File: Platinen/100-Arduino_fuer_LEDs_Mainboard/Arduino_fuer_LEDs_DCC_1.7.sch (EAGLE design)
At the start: 115 parts, among them IC1 7805, IC2 LM393N, J1 Tag/Nacht, U1 WS2812_MODUL, U2 LED NANO, U3 DCC NANO, U4 WS2812_MODUL, X1 RJ10, X2 AK500/2+M, X3 MAB 5SH Conrad: 738247 - VQ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

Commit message: New Mainboard V.:1.7
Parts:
- added IC3: 74LVC1G125DBV, 74xx-little-de:74LVC1G125DBV
- added R2: 47, rcl:R-EU_0204/7
- added R9: 10K, rcl:R-EU_0204/5
- added SJ2: SOLDERJUMPERNO, SparkFun-Retired:SOLDERJUMPERNO
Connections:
- removed net N$53: O4.4
- new net N$22: O3.4, O4.2
- new net N$31: IC3A.I, R26.2, SJ2.1, U3.TX0
- new net N$33: IC3A.O, R2.1
- new net N$34: R2.2, SJ2.2, U2.RX1
- net +5V: now also R9.2
- net N$3: now also IC3A.OE, R9.1, U3.A5; no longer R26.2, U2.RX1, U3.TX0
- net N$52: now also O4.4; no longer O3.4, O4.2
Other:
- note added: "Revision History: 31.08.20: - Corrected the LED PCBs (Ver. 1.5 was totaly wrong) - swaped the Input/Output pins (3-Pin header = Input) - corrected the pin assignement of the 3535 WS2812 18.10.20: - Corrected the output of the last connector"
- note added: "SJ2 ist normalerweise verbunden. IC3, R2 und R9 können anstelle von R26 bestückt werden. Dann bleibt SJ2 offen. (Noch nicht getestet)"
- note added: "Ver.: 1.7"
- note removed: "Revision History: 31.08.20: - Corrected the LED PCBs (Ver. 1.5 was totaly wrong) - swaped the Input/Output pins (3-Pin header = Input) - corrected the pin assignement of the 3535 WS2812"
- note removed: "Ver.: 1.6"
- moved on the sheet: IC2A, IC2B, R21, R22, R23, R24, R25, R26, R28, SJ_SX1, SJ_SX2, SJ_SX3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

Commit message: Moved IC3
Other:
- note added: "Achtung: Selectrix Empfang funktioniert NICHT wenn der DCC Optokoppler OK1 eingesteckt ist!"
- note added: "Ver.: 1.7.1"
- note added: "Wenn die Platine aus dem DCC Signal versorgt wird (IC1... bestückt), dann kann OK1 entfallen. Stattdessen wird eine Diode Pin3 nach Pin2 verwendet und NO_OPTO verbunden. R8 muss dann mit 33K bestückt werden. (Noch nicht getestet)"
- note removed: "Ver.: 1.7"
- note removed: "Wenn die Platine aus dem DCC Signal versorgt wird (IC1... bestückt), dann kann OK1 entfallen. Stattdessen wird eine Diode Pin3 nach Pin2 verwendet und NO_OPTO verbunden."
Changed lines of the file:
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@@
 <grid distance="0.1" unitdist="inch" unit="inch" style="lines" multiple="1" display="no" altdistance="0.05" altunitdist="inch" altunit="inch"/>
 <layers>
-<layer number="1" name="Top" color="4" fill="1" visible="yes" active="no"/>
-<layer number="16" name="Bottom" color="1" fill="1" visible="yes" active="no"/>
-<layer number="17" name="Pads" color="2" fill="1" visible="yes" active="no"/>
-<layer number="18" name="Vias" color="2" fill="1" visible="yes" active="no"/>
-<layer number="19" name="Unrouted" color="6" fill="1" visible="yes" active="no"/>
-<layer number="20" name="Dimension" color="24" fill="1" visible="yes" active="no"/>
-<layer number="21" name="tPlace" color="7" fill="1" visible="yes" active="no"/>
-<layer number="22" name="bPlace" color="7" fill="1" visible="yes" active="no"/>
-<layer number="23" name="tOrigins" color="15" fill="1" visible="yes" active="no"/>
-<layer number="24" name="bOrigins" color="15" fill="1" visible="yes" active="no"/>
-<layer number="25" name="tNames" color="7" fill="1" visible="yes" active="no"/>
-<layer number="26" name="bNames" color="7" fill="1" visible="yes" active="no"/>
-<layer number="27" name="tValues" color="7" fill="1" visible="yes" active="no"/>
-<layer number="28" name="bValues" color="7" fill="1" visible="yes" active="no"/>
+<layer number="1" name="Top" color="4" fill="1" visible="no" active="no"/>
+<layer number="16" name="Bottom" color="1" fill="1" visible="no" active="no"/>
+<layer number="17" name="Pads" color="2" fill="1" visible="no" active="no"/>
+<layer number="18" name="Vias" color="2" fill="1" visible="no" active="no"/>
+<layer number="19" name="Unrouted" color="6" fill="1" visible="no" active="no"/>
+<layer number="20" name="Dimension" color="24" fill="1" visible="no" active="no"/>
+<layer number="21" name="tPlace" color="7" fill="1" visible="no" active="no"/>
+<layer number="22" name="bPlace" color="7" fill="1" visible="no" active="no"/>
+<layer number="23" name="tOrigins" color="15" fill="1" visible="no" active="no"/>
+<layer number="24" name="bOrigins" color="15" fill="1" visible="no" active="no"/>
+<layer number="25" name="tNames" color="7" fill="1" visible="no" active="no"/>
+<layer number="26" name="bNames" color="7" fill="1" visible="no" active="no"/>
+<layer number="27" name="tValues" color="7" fill="1" visible="no" active="no"/>
+<layer number="28" name="bValues" color="7" fill="1" visible="no" active="no"/>
 <layer number="29" name="tStop" color="7" fill="3" visible="no" active="no"/>
 <layer number="30" name="bStop" color="7" fill="6" visible="no" active="no"/>
@@
 <layer number="35" name="tGlue" color="7" fill="4" visible="no" active="no"/>
 <layer number="36" name="bGlue" color="7" fill="5" visible="no" active="no"/>
-<layer number="37" name="tTest" color="7" fill="1" visible="yes" active="no"/>
-<layer number="38" name="bTest" color="7" fill="1" visible="yes" active="no"/>
+<layer number="37" name="tTest" color="7" fill="1" visible="no" active="no"/>
+<layer number="38" name="bTest" color="7" fill="1" visible="no" active="no"/>
 <layer number="39" name="tKeepout" color="4" fill="11" visible="no" active="no"/>
 <layer number="40" name="bKeepout" color="1" fill="11" visible="no" active="no"/>
@@
 <layer number="44" name="Drills" color="7" fill="1" visible="no" active="no"/>
 <layer number="45" name="Holes" color="7" fill="1" visible="no" active="no"/>
-<layer number="46" name="Milling" color="3" fill="1" visible="yes" active="no"/>
-<layer number="47" name="Measures" color="7" fill="1" visible="yes" active="no"/>
-<layer number="48" name="Document" color="7" fill="1" visible="yes" active="no"/>
-<layer number="49" name="Reference" color="7" fill="1" visible="yes" active="no"/>
-<layer number="50" name="dxf" color="7" fill="1" visible="yes" active="no"/>
-<layer number="51" name="tDocu" color="7" fill="1" visible="yes" active="no"/>
-<layer number="52" name="bDocu" color="7" fill="1" visible="yes" active="no"/>
-<layer number="53" name="tGND_GNDA" color="7" fill="9" visible="yes" active="no"/>
-<layer number="54" name="bGND_GNDA" color="1" fill="9" visible="yes" active="no"/>
-<layer number="56" name="wert" color="7" fill="1" visible="yes" active="no"/>
-<layer number="57" name="tCAD" color="7" fill="1" visible="yes" active="no"/>
-<layer number="59" name="tCarbon" color="7" fill="1" visible="yes" active="no"/>
-<layer number="60" name="bCarbon" color="7" fill="1" visible="yes" active="no"/>
+<layer number="46" name="Milling" color="3" fill="1" visible="no" active="no"/>
+<layer number="47" name="Measures" color="7" fill="1" visible="no" active="no"/>
+<layer number="48" name="Document" color="7" fill="1" visible="no" active="no"/>
+<layer number="49" name="Reference" color="7" fill="1" visible="no" active="no"/>
+<layer number="50" name="dxf" color="7" fill="1" visible="no" active="no"/>
+<layer number="51" name="tDocu" color="7" fill="1" visible="no" active="no"/>
+<layer number="52" name="bDocu" color="7" fill="1" visible="no" active="no"/>
+<layer number="53" name="tGND_GNDA" color="7" fill="9" visible="no" active="no"/>
+<layer number="54" name="bGND_GNDA" color="1" fill="9" visible="no" active="no"/>
+<layer number="56" name="wert" color="7" fill="1" visible="no" active="no"/>
+<layer number="57" name="tCAD" color="7" fill="1" visible="no" active="no"/>
+<layer number="59" name="tCarbon" color="7" fill="1" visible="no" active="no"/>
+<layer number="60" name="bCarbon" color="7" fill="1" visible="no" active="no"/>
 <layer number="88" name="SimResults" color="9" fill="1" visible="yes" active="yes"/>
 <layer number="89" name="SimProbes" color="9" fill="1" visible="yes" active="yes"/>
@@
 <text x="48.26" y="121.92" size="1.778" layer="97" rot="R90">A6, A7: No Din/Dout
             No Pullup</text>
-<text x="238.76" y="-15.24" size="3.81" layer="97">Ver.: 1.7</text>
+<text x="238.76" y="-15.24" size="3.81" layer="97">Ver.: 1.7.1</text>
 <wire x1="-81.28" y1="198.12" x2="-81.28" y2="200.66" width="0.1524" layer="97"/>
 <wire x1="-81.28" y1="200.66" x2="-82.042" y2="201.422" width="0.1524" layer="97"/>
@@
                =&gt; Ver. 1.6
 10.09.20: - Changed LM293 comment
-18.10.20: - Added optional buffer IC3</text>
+18.10.20: - Added optional buffer IC3
+29.01.21: =&gt; Vwr.: 1.7.1
+                - moved IC3 (problem with narrow pads)</text>
 <text x="-91.44" y="31.75" size="1.778" layer="91">O2</text>
 <text x="-91.44" y="16.51" size="1.778" layer="91">O1</text>
@@
 SJ_SX3 verbinden wenn die Platine aus dem SX Bus versorgt werden soll.
 Das geht aber nur bei wenigen LEDs.</text>
-<text x="-68.58" y="83.82" size="1.524" layer="97" align="top-left">Wenn die Platine aus dem DCC Signal versorgt wird (IC1... bestückt),
+<text x="-68.58" y="86.36" size="1.524" layer="97" align="top-left">Wenn die Platine aus dem DCC Signal versorgt wird (IC1... bestückt),
 dann kann OK1 entfallen. Stattdessen wird eine Diode Pin3 nach Pin2
-verwendet und NO_OPTO verbunden.</text>
+verwendet und NO_OPTO verbunden.
+R8 muss dann mit 33K bestückt werden. (Noch nicht getestet)</text>
 <text x="113.03" y="36.83" size="1.778" layer="97">Achtung: der LM293N
 kann NICHT benutzt
@@
 (Noch nicht getestet)
 </text>
+<text x="33.02" y="-12.7" size="1.524" layer="97" align="top-left">Achtung: Selectrix Empfang funktioniert
+NICHT wenn der DCC Optokoppler OK1
+eingesteckt ist!
+</text>
 </plain>

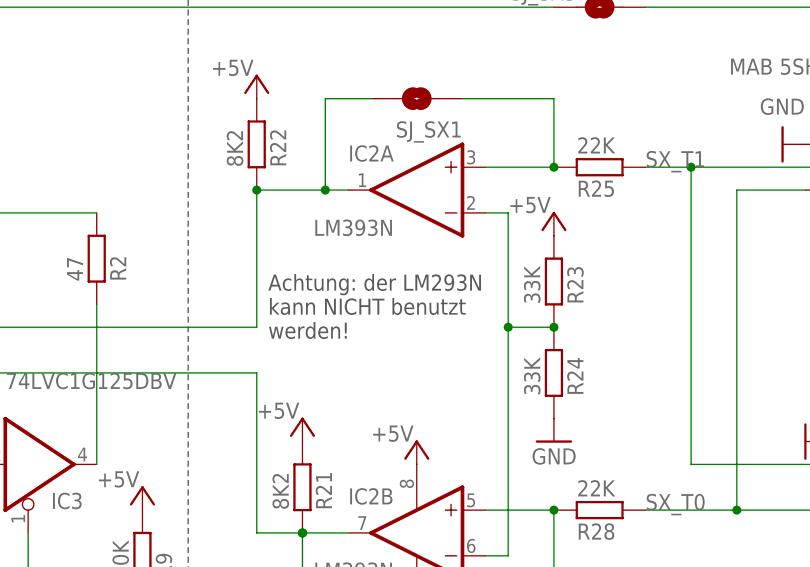
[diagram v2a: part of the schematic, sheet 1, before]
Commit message: Korrigiert: LM292 kann nicht verwendet werden
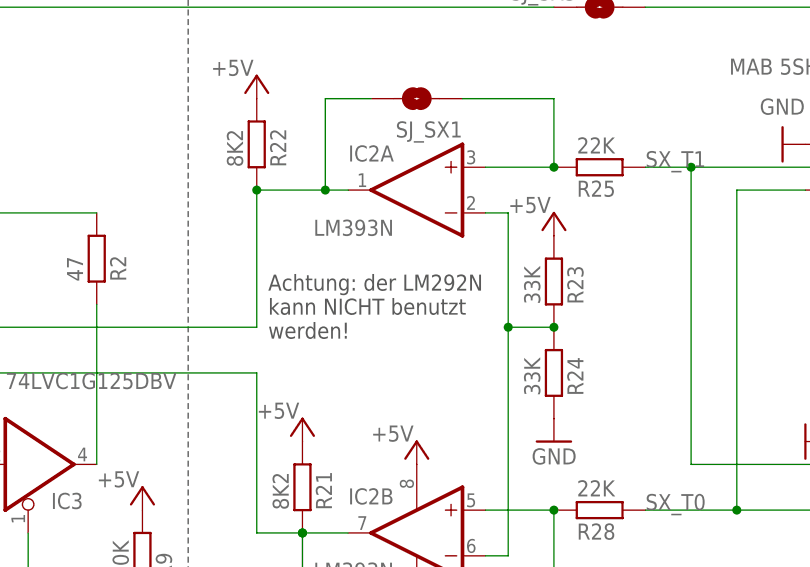
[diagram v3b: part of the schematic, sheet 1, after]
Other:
- note added: "Achtung: der LM292N kann NICHT benutzt werden!"
- note removed: "Achtung: der LM293N kann NICHT benutzt werden!"
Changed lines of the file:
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@@
 verwendet und NO_OPTO verbunden.
 R8 muss dann mit 33K bestückt werden. (Noch nicht getestet)</text>
-<text x="113.03" y="36.83" size="1.778" layer="97">Achtung: der LM293N
+<text x="113.03" y="36.83" size="1.778" layer="97">Achtung: der LM292N
 kann NICHT benutzt
 werden!</text>
